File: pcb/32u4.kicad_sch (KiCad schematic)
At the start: 100 parts, among them SW0 SW_SPST, SW1 SW_SPST, SW1.0 SW_SPST, SW1.1 SW_SPST, SW1.2 SW_SPST, SW10 SW_SPST, SW11 SW_SPST, SW110 SW_SPST, SW111 SW_SPST, SW13 SW_SPST, SW14 SW_SPST, SW15 SW_SPST, SW16 SW_SPST, SW17 SW_SPST, SW18 SW_SPST, SW19 SW_SPST, SW2 SW_SPST, SW20 SW_SPST, SW21 SW_SPST, SW210 SW_SPST, SW211 SW_SPST, SW22 SW_SPST, SW23 SW_SPST, SW24 SW_SPST, SW25 SW_SPST, SW26 SW_SPST, SW27 SW_SPST, SW28 SW_SPST, SW29 SW_SPST, SW3 SW_SPST, SW30 SW_SPST, SW31 SW_SPST, SW310 SW_SPST, SW311 SW_SPST, SW32 SW_SPST, SW33 SW_SPST, SW34 SW_SPST, SW35 SW_SPST, SW36 SW_SPST, SW37 SW_SPST, SW38 SW_SPST, SW39 SW_SPST, SW4 SW_SPST, SW40 SW_SPST, SW41 SW_SPST, SW411 SW_SPST, SW42 SW_SPST, SW44 SW_SPST, SW45 SW_SPST, SW46 SW_SPST, SW47 SW_SPST, SW49 SW_SPST, SW5 SW_SPST, SW55 SW_SPST, SW56 SW_SPST, SW6 SW_SPST, SW7 SW_SPST, SW8 SW_SPST, SW9 SW_SPST

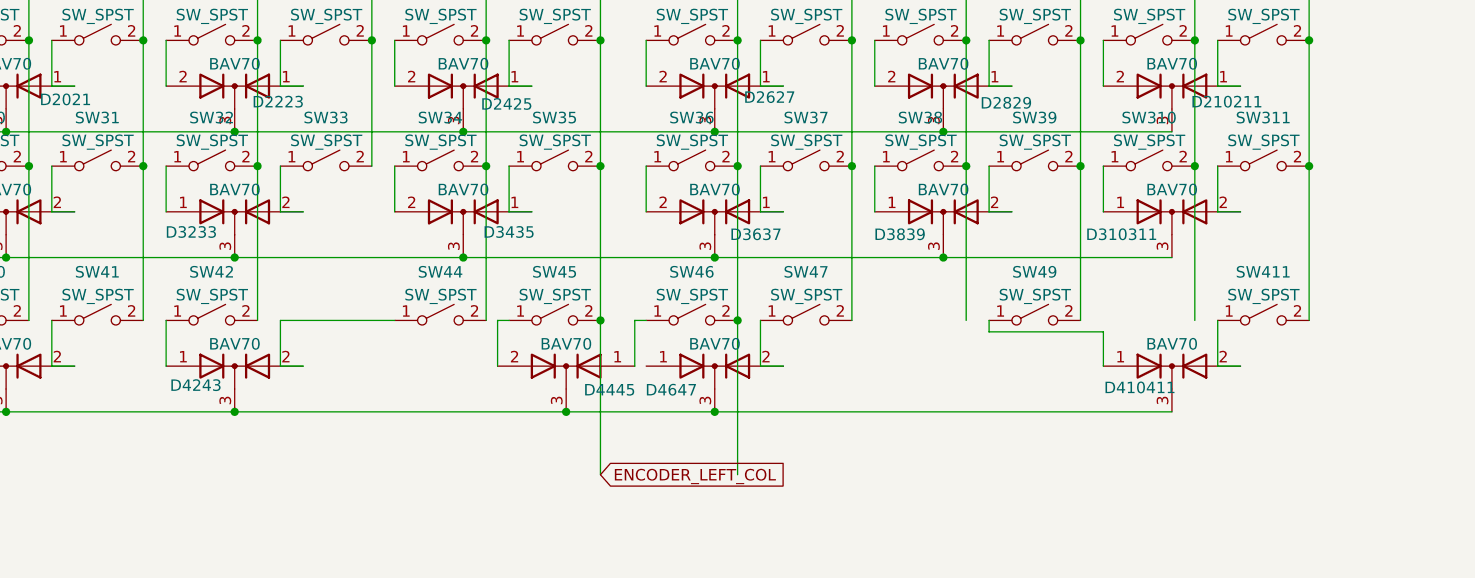
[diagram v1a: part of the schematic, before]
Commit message: updated layout options and pcb
- updated gerber and assembly files
- updated layout options image
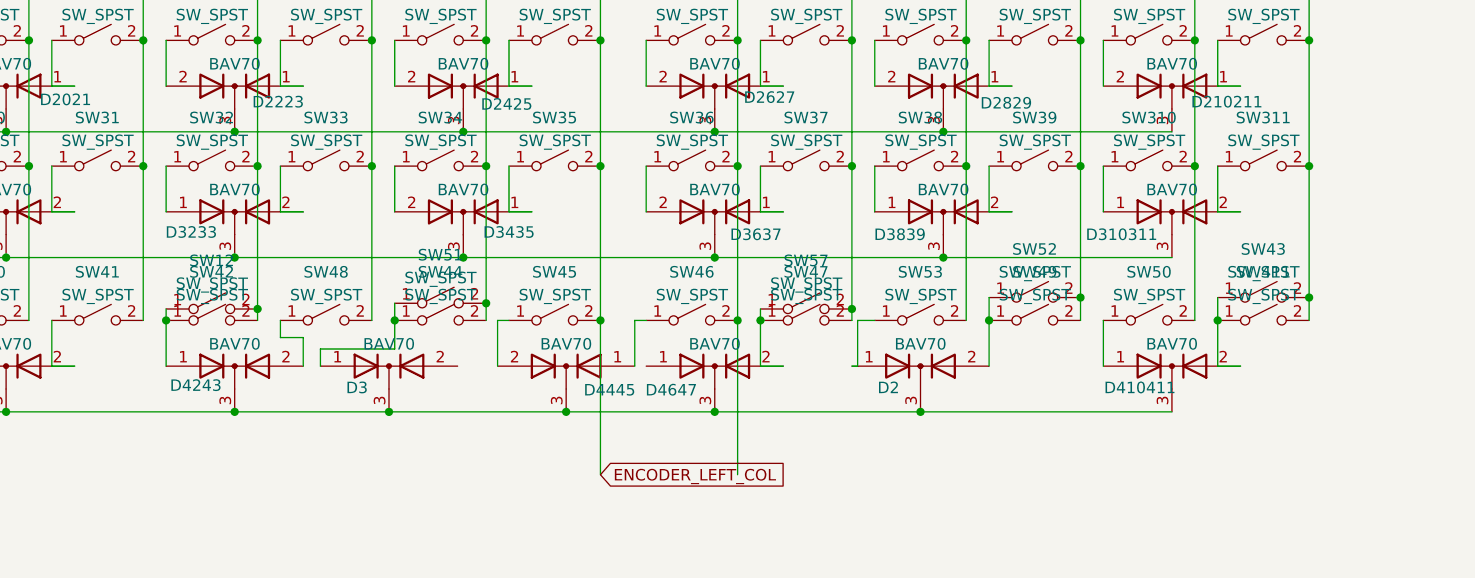
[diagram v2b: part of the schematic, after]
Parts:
- added D2, D3: BAV70, Package_TO_SOT_SMD:SOT-23, symbol Diode:BAV70
- added SW12, SW43, SW48, SW50, SW51, SW52, SW53, SW57: SW_SPST, Keebio-Parts:MX-Alps-Choc-1U-NoLED, symbol Switch:SW_SPST
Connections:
- net COL10: now also SW50.2 (B)
- net COL11: now also SW43.2 (B)
- net COL2: now also SW12.2 (B)
- net COL3: now also SW48.2 (B)
- net COL4: now also SW51.2 (B)
- net COL7: now also SW57.2 (B)
- net COL8: now also SW53.2 (B)
- net COL9: now also SW52.2 (B)
- net ROW4: now also D2.3 (K), D3.3 (K)
- net at D4243.2 (A): now also SW48.1 (A); no longer SW44.1 (A)
- net at D4243.1 (A), SW42.1 (A): now also SW12.1 (A)
- net at D4647.2 (A), SW47.1 (A): now also SW57.1 (A)
- net at D410411.2 (A), SW411.1 (A): now also SW43.1 (A)
- net at SW49.1 (A): now also D2.2 (A), SW52.1 (A); no longer D410411.1 (A)
- new net: D2.1 (A), SW53.1 (A)
- new net: D3.1 (A), SW44.1 (A), SW51.1 (A)
- new net: D410411.1 (A), SW50.1 (A)
